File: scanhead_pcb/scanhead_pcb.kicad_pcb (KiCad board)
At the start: 2 copper layers, 35.1 x 32.8 mm, 20 parts, among them J1 MOLEX_2031, J2 10pinIDC, J4 MOLEX_2051, J5 MOLEX_2031, J6 MOLEX_2021, J7 MOLEX_2021, Q1 IRFML8244, U1 DIGIPOT_50K, U2 U_IC-HKB

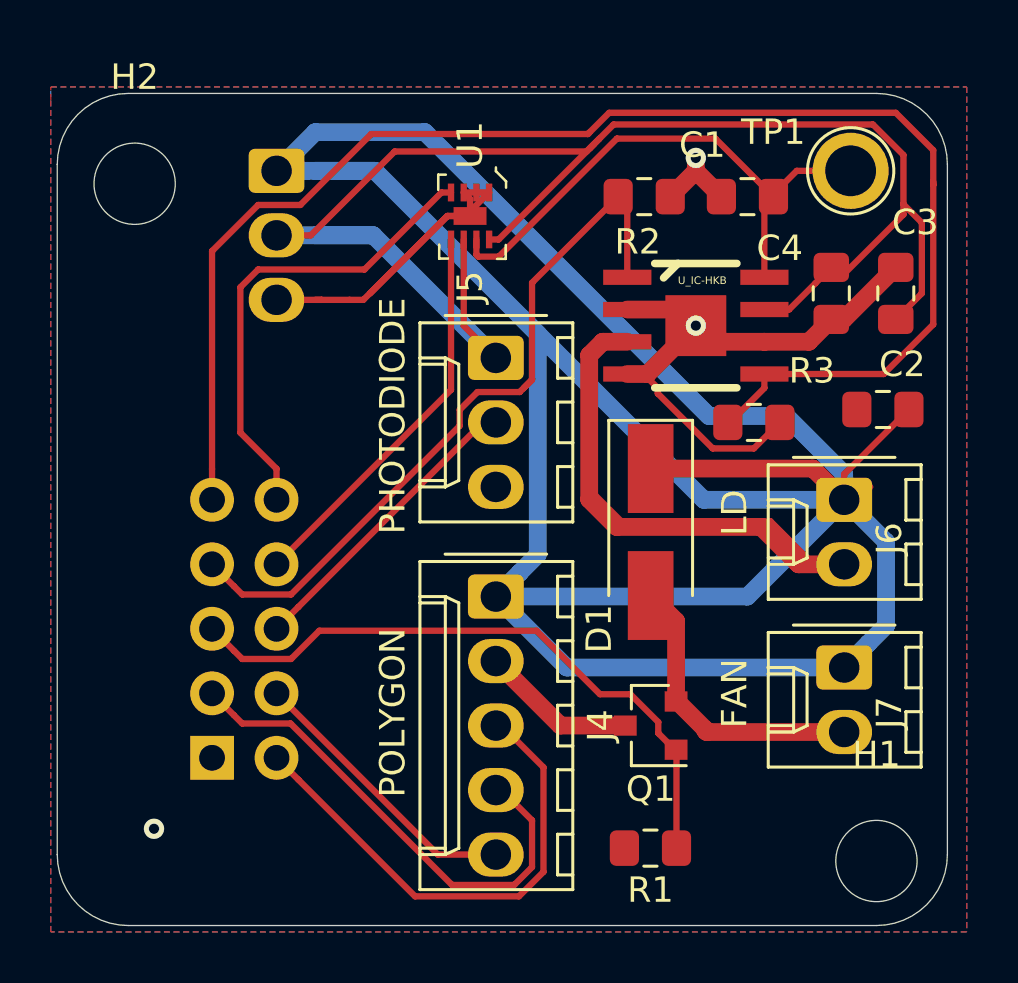
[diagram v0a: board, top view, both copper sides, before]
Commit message: changed most cables to flatex or jumper wire moved from 1 diode to 2 diodes added spi readout chip for photodiode photodiode is now surface mount
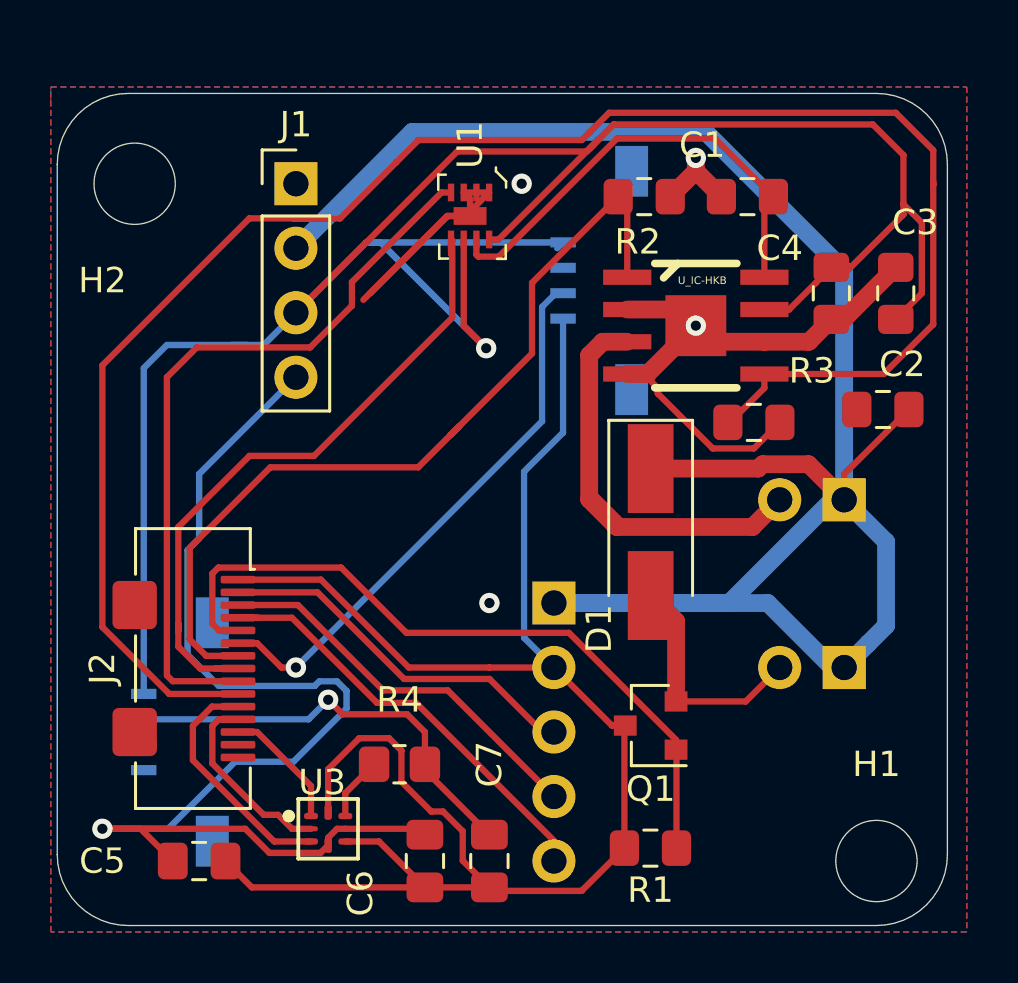
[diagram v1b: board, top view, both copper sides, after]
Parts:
- removed TP1: TestPoint, TestPoint:TestPoint_Plated_Hole_D2.0mm
- added C5: 1uF, Capacitor_SMD:C_0805_2012Metric_Pad1.18x1.45mm_HandSolder, F.Cu at (39.4, -21.6)
- added C6: 1uF, Capacitor_SMD:C_0805_2012Metric_Pad1.18x1.45mm_HandSolder, F.Cu at (48.3, -21.6)
- added C7: 1uF, Capacitor_SMD:C_0805_2012Metric_Pad1.18x1.45mm_HandSolder, F.Cu at (50.8, -21.6)
- added J3: FPC molex 4 pin, Connector_FFC-FPC:Molex_200528-0040_1x04-1MP_P1.00mm_Horizontal, B.Cu at (54.6, -44.5)
- added R4: 0K, Resistor_SMD:R_0805_2012Metric_Pad1.20x1.40mm_HandSolder, F.Cu at (47.3, -25.4)
- added U3: NCD98011, sockets_scanhead:Texas_Instruments-X2QFN8-0-0-0, F.Cu at (44.5, -22.9)
- J1: value MOLEX_2031 -> Jumper wire 4 pin; footprint Connector_Molex:Molex_KK-254_AE-6410-03A_1x03_P2.54mm_Vertical -> Connector_PinHeader_2.54mm:PinHeader_1x04_P2.54mm_Vertical; moved to F.Cu
- J2: value 10pinIDC -> FPC 15 pin molex vertical; footprint Connector_IDC:IDC-Header_2x05_P2.54mm_Vertical -> Connector_FFC-FPC:Molex_502231-1500_1x15-1SH_P0.5mm_Vertical; moved to F.Cu
- J4: value MOLEX_2051 -> jumper wire 5 pin; footprint Connector_Molex:Molex_KK-254_AE-6410-05A_1x05_P2.54mm_Vertical -> Connector_PinHeader_2.54mm:PinHeader_1x05_P2.54mm_Vertical; moved to B.Cu
- J5: value MOLEX_2031 -> FPC molex 4 pin; footprint Connector_Molex:Molex_KK-254_AE-6410-03A_1x03_P2.54mm_Vertical -> Connector_FFC-FPC:Molex_200528-0040_1x04-1MP_P1.00mm_Horizontal; moved to B.Cu
- J6, J7: value MOLEX_2021 -> jumper wire 2 pin; footprint Connector_Molex:Molex_KK-254_AE-6410-02A_1x02_P2.54mm_Vertical -> Connector_PinHeader_2.54mm:PinHeader_1x02_P2.54mm_Vertical; moved to B.Cu
- moved J5 19.6 mm to (38.1, -26.7)
- moved J2 3.52 mm to (39.9, -29.2), turned to 270 degrees
- moved J4 2.30 mm to (53.3, -31.8), turned to 180 degrees
- moved J1 0.92 mm to (43.2, -48.3), turned to 0 degrees
- turned J6 to 90 degrees
- turned J7 to 90 degrees
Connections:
- J1 pad 1: +12V -> GND
- J1 pad 2: +5V -> +12V
- J1 pad 3: GND -> +5V
- J2 pad 10: POT_SDA -> IC_HB_PWM1
- J2 pad 6: PH_DIODE -> DIGITAL1
- J2 pad 9: IC_HB_PWM1 -> POT_SDA
- J5 pad 2: PH_DIODE -> ANALOG2
- J5 pad 3: GND -> Net-(J5-Pad3)
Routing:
- net GND: track 50.8 -> 111.5 mm, vias 3 -> 4
- net +3V3: track 0.00 -> 49.0 mm, vias 0 -> 1
- net +12V: track 123.5 -> 81.2 mm
- net +5V: track 65.4 -> 98.3 mm, vias 0 -> 1
- net DIGITAL1: track 0.00 -> 21.9 mm, vias 0 -> 1
- net ANALOG2: track 0.00 -> 17.0 mm, vias 0 -> 1
- net IC_HB_PWM1: track 58.2 -> 72.4 mm
- net LDK: track 36.7 -> 24.2 mm
- net PH_DIODE: track 12.0 -> 0.00 mm
- net POT_SCL: track 15.6 -> 26.5 mm
- net POT_SDA: track 18.8 -> 29.4 mm
- net SPI_CLK: track 0.00 -> 9.42 mm
- net SPI_OUT: track 0.00 -> 7.58 mm
- net POLY_PWM: track 11.3 -> 17.7 mm
- net POLY_EN: track 19.8 -> 14.6 mm
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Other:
- board text added: "LASER"
- board text added: "PHOTODIODE1"
- board text added: "PHOTODIODE2"
- board text removed: "LD"
- board text removed: "PHOTODIODE"

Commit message: updated all boards
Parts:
- added F1: 1A, Fuse:Fuse_1206_3216Metric, F.Cu at (51.2, -34.4)
- added F2: 2A, Fuse:Fuse_1206_3216Metric, F.Cu at (51.2, -36.8)
- added F3: 3A, Fuse:Fuse_1206_3216Metric, F.Cu at (51.2, -39.2)
- J1: value Jumper wire 4 pin -> Screw_Terminal_01x04; footprint Connector_PinHeader_2.54mm:PinHeader_1x04_P2.54mm_Vertical -> TerminalBlock_Phoenix:TerminalBlock_Phoenix_MPT-0,5-4-2.54_1x04_P2.54mm_Horizontal
- J3, J5: footprint Connector_FFC-FPC:Molex_200528-0040_1x04-1MP_P1.00mm_Horizontal -> sockets_scanhead:Molex_200528-0040_1x04-1MP_P1.00mm_Horizontal
- moved J1 3.29 mm to (43.8, -45.0), turned to 270 degrees
- moved J3 1.86 mm to (56.4, -44.0), turned to 90 degrees
- moved J5 1.27 mm to (39.4, -26.7), turned to 90 degrees
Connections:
- J1 pad 2: +12V -> Net-(F3-Pad2)
- J1 pad 3: +5V -> Net-(F2-Pad1)
- J1 pad 4: +3V3 -> Net-(F1-Pad2)
- J2 pad 1: GND -> Net-(J2-Pad1)
- J3 pad 1: +5V -> GND
- J3 pad 4: GND -> +5V
- J5 pad 1: +5V -> GND
- J5 pad 4: GND -> +5V
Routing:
- net +3V3: track 49.0 -> 24.9 mm, vias 1 -> 2
- net +12V: track 81.2 -> 58.7 mm, vias 0 -> 3
- net +5V: track 98.3 -> 120.7 mm, vias 1 -> 3
- net IC_HB_PWM1: track 72.4 -> 82.3 mm
- net Net-(F3-Pad2): track 0.00 -> 9.50 mm
- net POT_SCL: track 26.5 -> 34.9 mm
- net Net-(F2-Pad1): track 0.00 -> 7.41 mm
- net Net-(F1-Pad2): track 0.00 -> 7.36 mm
- net IC_HB_PWM2: track 33.8 -> 40.1 mm
- net GND: track 111.5 -> 116.2 mm, vias 4 -> 3
- net ANALOG2: track 17.0 -> 13.3 mm
- net DIGITAL1: track 21.9 -> 24.0 mm
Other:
- board text added: "12V"
- board text added: "3V"
- board text added: "5V"
- board text added: "GND"

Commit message: updated bom
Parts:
- J1: footprint TerminalBlock_Phoenix:TerminalBlock_Phoenix_MPT-0,5-4-2.54_1x04_P2.54mm_Horizontal -> Connector_Molex:Molex_KK-254_AE-6410-04A_1x04_P2.54mm_Vertical
- J2: footprint Connector_FFC-FPC:Molex_502231-1500_1x15-1SH_P0.5mm_Vertical -> sockets_scanhead:TE_1-1734248-5
- moved J1 4.24 mm to (44.7, -40.9)
- moved C5 4.02 mm to (43.2, -20.3)
- moved J2 2.72 mm to (38.1, -31.2)
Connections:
- J2 pad 1: Net-(J2-Pad1) -> POLY_EN
- J2 pad 14: Net-(J2-Pad14) -> SPI_CSN
- J2 pad 15: Net-(J2-Pad15) -> SPI_CSN
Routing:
- net +5V: track 120.7 -> 91.7 mm
- net POLY_PWM: track 17.7 -> 32.7 mm
- net POLY_EN: track 14.6 -> 29.4 mm
- net SPI_CSN: track 4.94 -> 17.6 mm
- net FAN_PWM: track 28.6 -> 39.5 mm, vias 0 -> 2
- net SPI_OUT: track 7.58 -> 18.0 mm
- net SPI_CLK: track 9.42 -> 19.8 mm
- net POLY_READY: track 15.6 -> 24.2 mm
- net +12V: track 58.7 -> 66.8 mm
- net DIGITAL1: track 24.0 -> 31.1 mm
- net IC_HB_PWM2: track 40.1 -> 33.1 mm, vias 0 -> 2
- net GND: track 116.2 -> 110.2 mm
- net Net-(F3-Pad2): track 9.50 -> 5.48 mm
- net IC_HB_PWM1: track 82.3 -> 78.6 mm
- net +3V3: track 24.9 -> 21.5 mm
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
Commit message: new boards
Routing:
- net GND: track 110.2 -> 116.4 mm, vias 3 -> 10
- net IC_HB_PWM1: track 78.6 -> 74.0 mm
- net +5V: track 91.7 -> 88.3 mm

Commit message: updated bom
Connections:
- J2 pad 1: POLY_EN -> (no net)
- J2 pad 14: SPI_CSN -> (no net)
- J2 pad 14_1: SPI_CSN -> (no net)
- J2 pad 15: SPI_CSN -> (no net)
- J2 pad 15_1: SPI_CSN -> (no net)
- J2 pad 1_1: POLY_EN -> (no net)
- J3 pad 2: Net-(J3-Pad2) -> (no net)
- J5 pad 3: Net-(J5-Pad3) -> (no net)
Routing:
- net SPI_CSN: track 17.6 -> 8.89 mm
- net POLY_EN: track 29.5 -> 24.7 mm

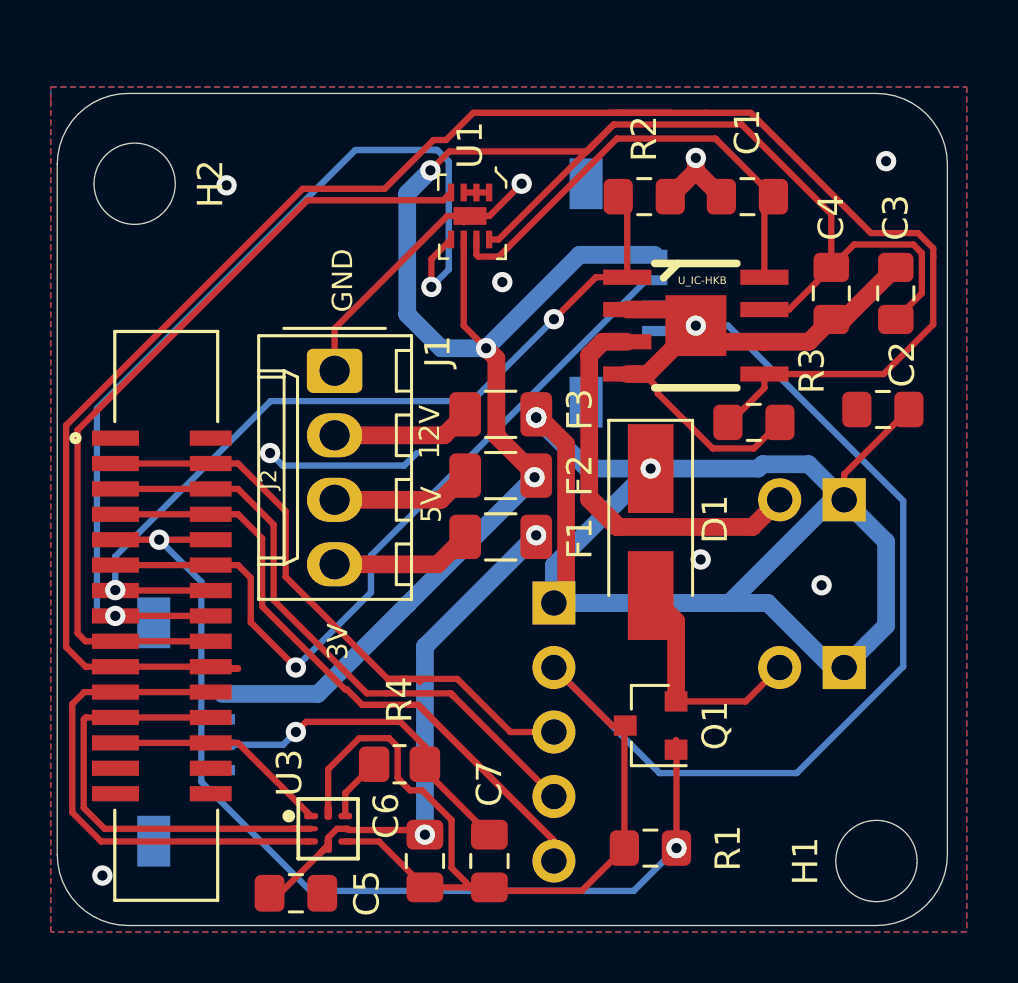
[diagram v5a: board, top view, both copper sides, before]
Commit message: fixed orientation connector laserdiode connector to correct side
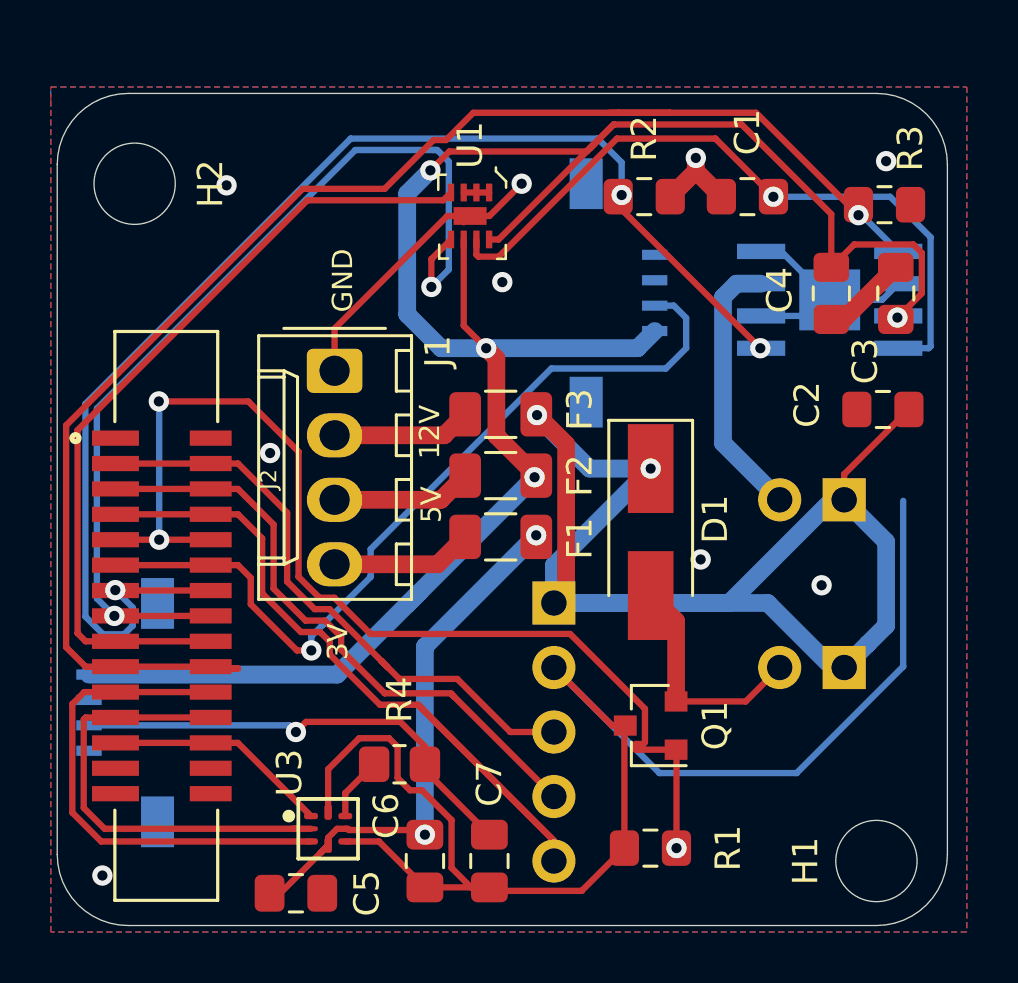
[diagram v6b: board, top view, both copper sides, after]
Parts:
- U2: moved to B.Cu
- moved R3 10.00 mm to (66.4, -47.4)
- moved U2 5.37 mm to (64.2, -43.7), turned to 90 degrees
- moved J5 3.51 mm to (35.9, -27.4), turned to 270 degrees
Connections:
- J3 pad 1: GND -> +5V
- J3 pad 2: (no net) -> DIGITAL1
- J3 pad 3: DIGITAL1 -> (no net)
- J3 pad 4: +5V -> GND
- J5 pad 1: GND -> +5V
- J5 pad 2: ANALOG2 -> (no net)
- J5 pad 3: (no net) -> ANALOG2
- J5 pad 4: +5V -> GND
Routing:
- net GND: track 116.4 -> 87.0 mm, vias 10 -> 9
- net IC_HB_PWM2: track 33.1 -> 52.1 mm, vias 2 -> 3
- net IC_HB_PWM1: track 74.0 -> 59.6 mm, vias 0 -> 1
- net LDK: track 24.2 -> 10.6 mm
- net POT_W: track 18.6 -> 28.3 mm, vias 0 -> 1
- net +12V: track 66.8 -> 58.4 mm, vias 3 -> 2
- net ANALOG2: track 13.3 -> 18.4 mm
- net +5V: track 88.3 -> 83.8 mm, vias 3 -> 4
- net FAN_PWM: track 39.5 -> 43.7 mm, vias 2 -> 3
- net DIGITAL1: track 31.1 -> 33.2 mm
- net POLY_EN: track 24.7 -> 23.6 mm
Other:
- board text added: "PHOTODIODE ANALOG"
- board text added: "PHOTODIODE DIGITAL"
- board text removed: "PHOTODIODE1"
- board text removed: "PHOTODIODE2"

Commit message: 3V routed via flatex
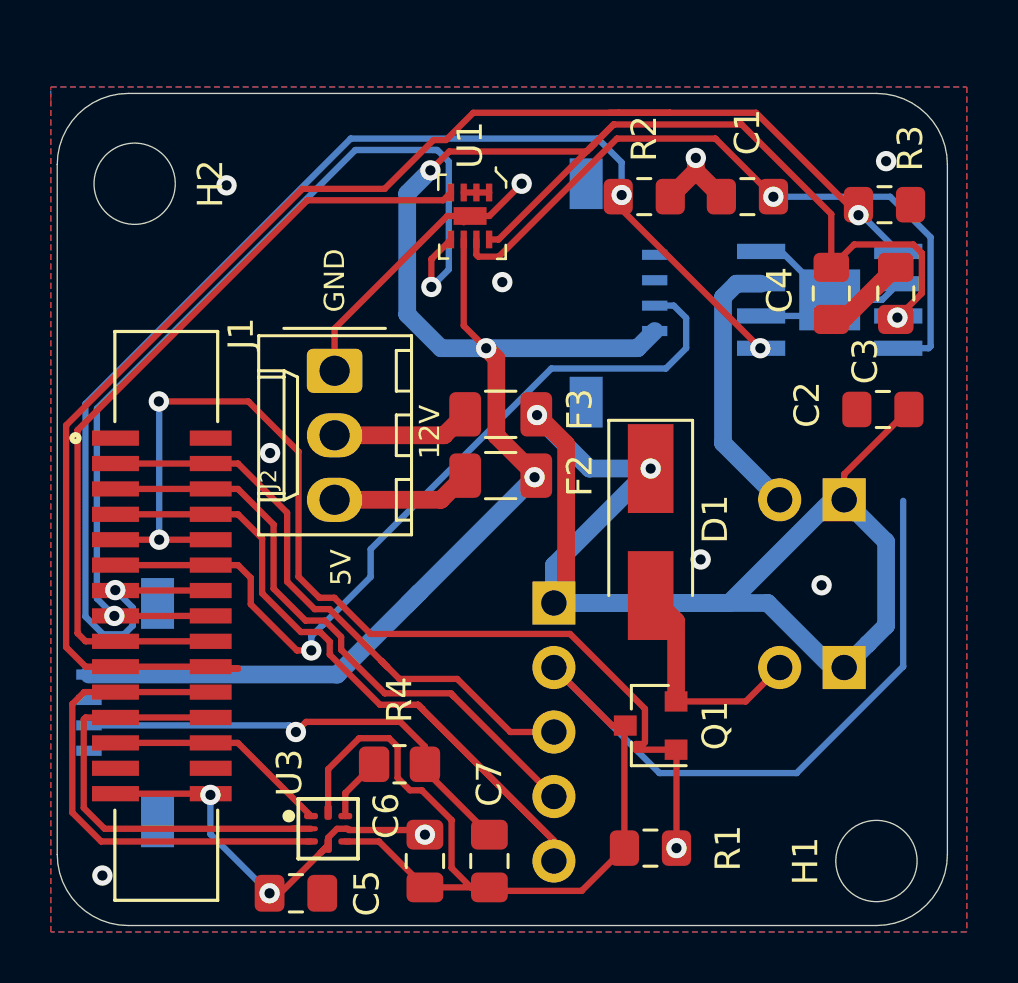
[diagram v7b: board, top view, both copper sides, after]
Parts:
- removed F1: 1A, Fuse:Fuse_1206_3216Metric
- J1: value Screw_Terminal_01x04 -> Screw_Terminal_01x03; footprint Connector_Molex:Molex_KK-254_AE-6410-04A_1x04_P2.54mm_Vertical -> Connector_Molex:Molex_KK-254_AE-6410-03A_1x03_P2.54mm_Vertical
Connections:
- J2 pad 15: (no net) -> +3V3
- J2 pad 15_1: (no net) -> +3V3
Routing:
- net Net-(F1-Pad2): track 5.59 -> 0.00 mm
- net +3V3: track 21.5 -> 16.5 mm, vias 2 -> 3
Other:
- board text removed: "3V"

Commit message: changes scanhead pcb
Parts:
- J4: footprint Connector_PinHeader_2.54mm:PinHeader_1x05_P2.54mm_Vertical -> Connector_Molex:Molex_KK-254_AE-6410-05A_1x05_P2.54mm_Vertical
- J6, J7: footprint Connector_PinHeader_2.54mm:PinHeader_1x02_P2.54mm_Vertical -> Connector_Molex:Molex_KK-254_AE-6410-02A_1x02_P2.54mm_Vertical
- moved J5 10.9 mm to (46.9, -26.9), turned to 90 degrees
- moved J6 1.02 mm to (64.7, -36.8), turned to 180 degrees
- turned J4 to 270 degrees
- turned J7 to 180 degrees
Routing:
- net GND: track 87.0 -> 63.7 mm
- net +5V: track 83.8 -> 76.2 mm
- net POLY_PWM: track 32.7 -> 25.8 mm
- net ANALOG2: track 18.4 -> 15.1 mm
- net +12V: track 58.4 -> 57.9 mm
